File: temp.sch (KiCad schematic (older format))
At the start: 27 parts, among them Q38 2N3904, U42 74LS32, U43 MCP6002, U44 74LS04, U45 74LS04, U46 74LS76, U47 74LS04, U48 74LS07, U49 74LS08, U50 7400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

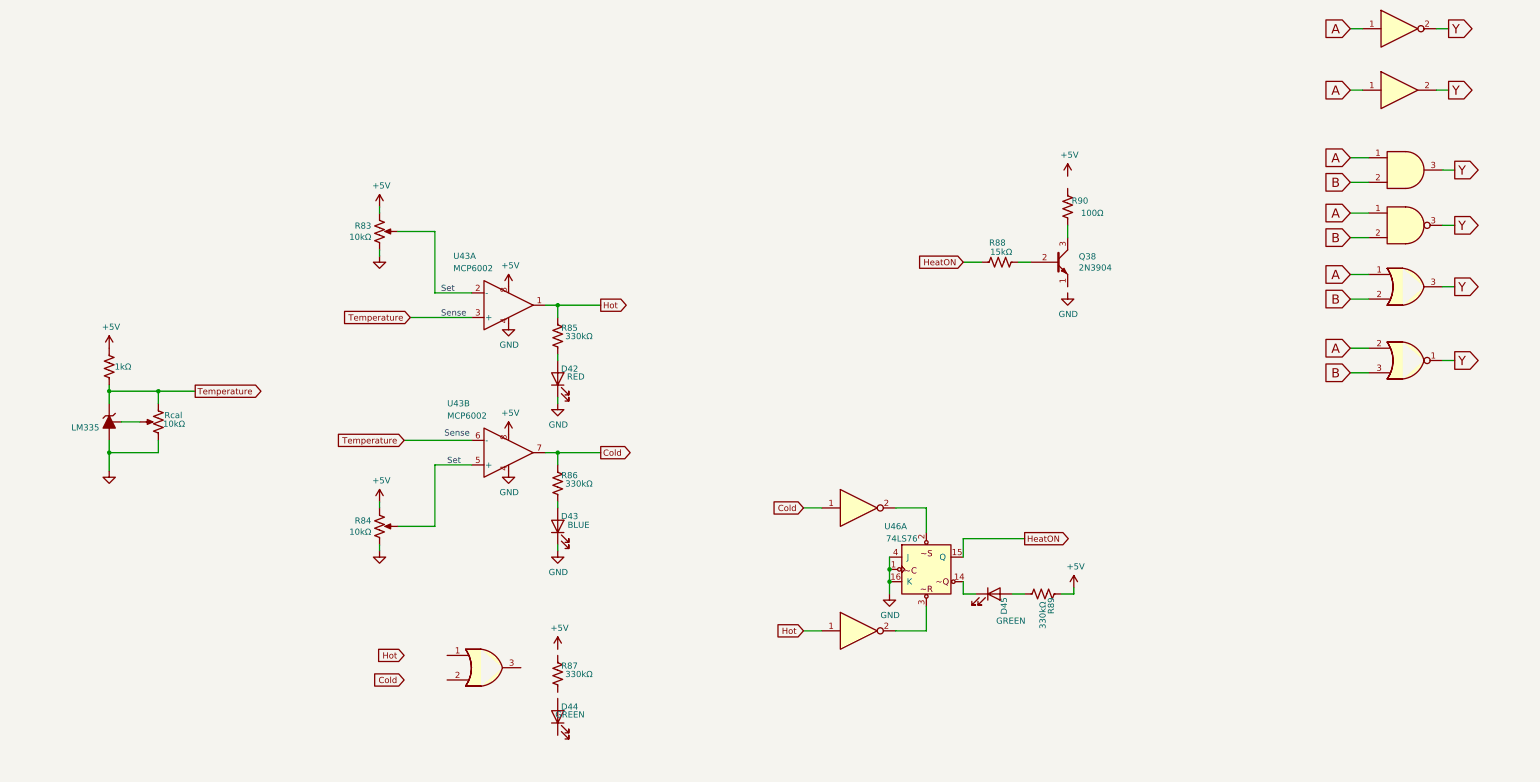
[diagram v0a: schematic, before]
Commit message: clean up schematic
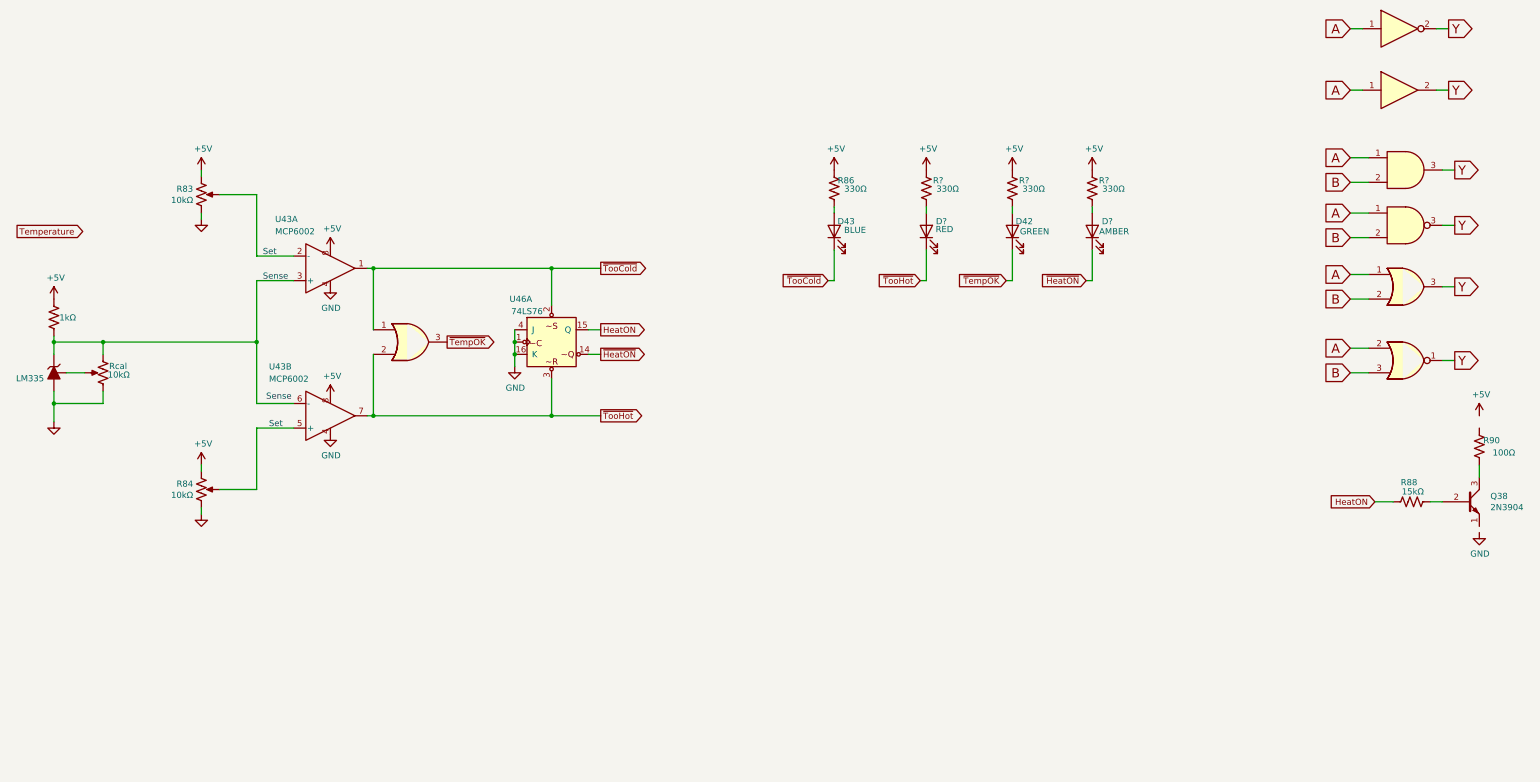
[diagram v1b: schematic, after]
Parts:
- removed D44, D45: GREEN, symbol Device:LED
- removed R85, R87, R89: 330kΩ, symbol Device:R_US
- removed U44, U45: 74LS04, symbol 74xx:74LS04
- added D?: RED, symbol Device:LED
- added D?: AMBER, symbol Device:LED
- added R? (x3): 330Ω, symbol Device:R_US
- D42: value RED -> GREEN
- R86: value 330kΩ -> 330Ω
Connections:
- net Hot is gone; now on net ~TooCold: U43.1
- net +5V: now also R86.2, R?.2, R?.2, R?.2
- net GND: no longer D42.1 (K), D43.1 (K)
- net Temperature: no longer R81.1, Rcal.3, Temp2.1 (K), U43.3 (+), U43.6 (-)
- net at D42.2 (A): now also R?.1
- net ~HeatON: now reaches U46.14
- net ~HeatON: now also D?.1 (K)
- net ~TooCold: now reaches U46.2
- net ~TooCold: now also D43.1 (K), U42.1
- net ~TooHot: now reaches U46.3
- net ~TooHot: now also U42.2, U43.7, D?.1 (K)
- net ~TempOK: now reaches U42.3
- net ~TempOK: now also D42.1 (K)
- removed net Cold: R86.2, U43.7
- new net: R81.1, Rcal.3, Temp2.1 (K), U43.3 (+), U43.6 (-)
- new net: D?.2 (A), R?.1 (x2)
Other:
- moved on the sheet: D42, D43, Q38, R83, R84, R86, R88, R90, Rcal, U43A, U43B, U46A

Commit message: add triac driver
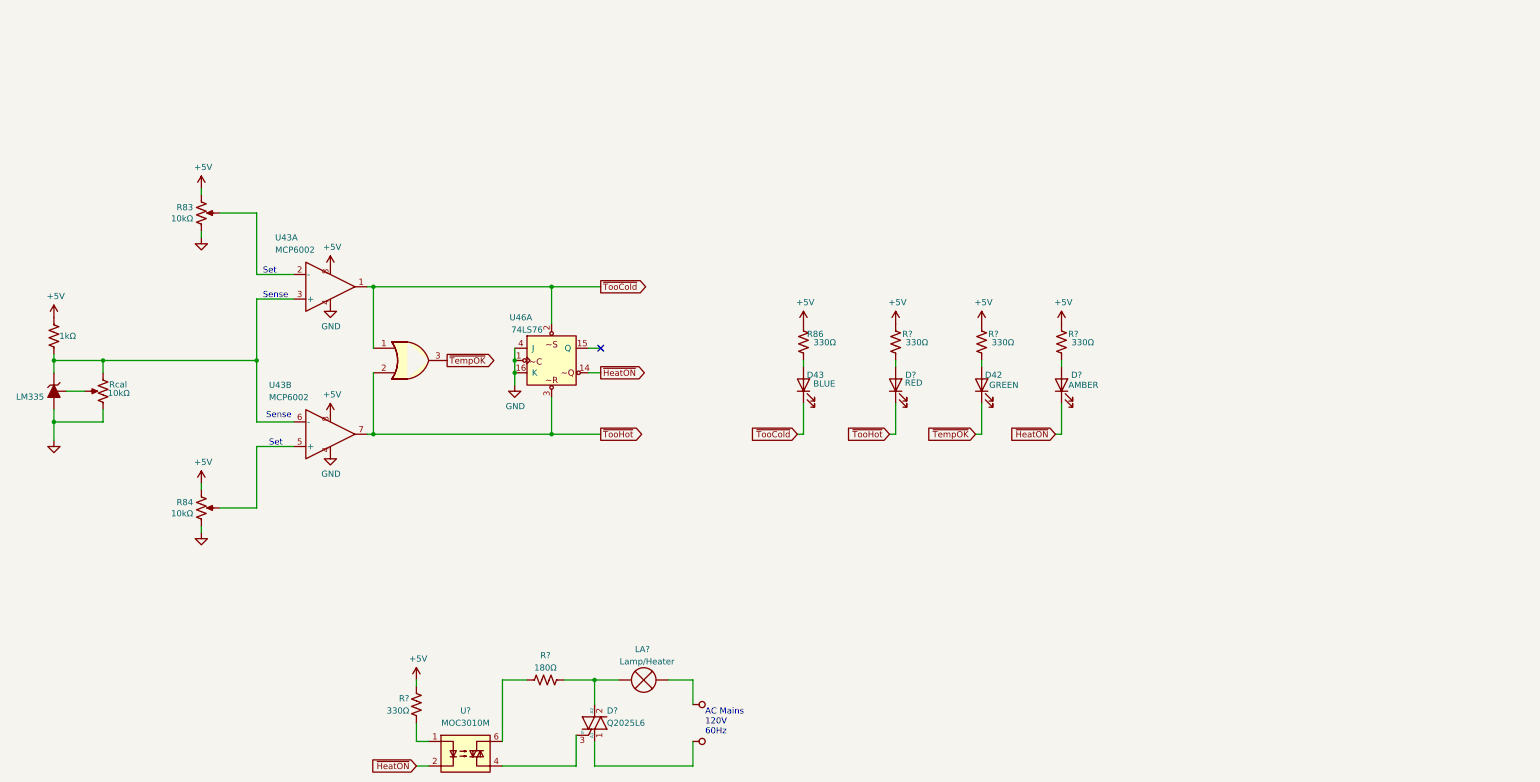
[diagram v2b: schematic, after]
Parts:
- removed Q38: 2N3904, Package_TO_SOT_THT:TO-92_Inline, symbol Transistor_BJT:2N3904
- removed R88: 15kΩ, symbol Device:R_US
- removed R90: 100Ω, symbol Device:R_US
- removed U47: 74LS04, symbol 74xx:74LS04
- removed U48: 74LS07, symbol 74xx:74LS07
- removed U49: 74LS08, symbol 74xx:74LS08
- removed U50: 7400, symbol 74xx:7400
- removed U51: 74LS32, symbol 74xx:74LS32
- removed U52: 7402, symbol 74xx:7402
- added D?: Q2025L6, symbol Device:Q_TRIAC_A1A2G
- added LA?: Lamp/Heater, symbol Device:Lamp
- added R?: 180Ω, symbol Device:R_US
- added R?: 330Ω, symbol Device:R_US
- added U?: MOC3010M, symbol Relay_SolidState:MOC3010M
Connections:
- net +5V: now also R?.2
- net ~HeatON: now also U?.2
- net HeatON: no longer names the net of U46.15 (Q)
- new net: D?.2 (A2), LA?.2 (+), R?.1
- new net: D?.3 (G), U?.4
- new net: R?.2, U?.6
- new net: R?.1, U?.1
- new net LINE: D?.1 (A1), LA?.1 (-)
- no-connect marks 0 -> 1
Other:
- note added: "AC Mains\n120V\n60Hz"
- moved on the sheet: D42, D43, D?, R83, R84, R86, R?, Rcal, U43A, U43B, U46A
